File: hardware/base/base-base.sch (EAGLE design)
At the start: 8 parts, among them U1 SD_CARD_SOCKET4UCON, X1 BU-SMA-V

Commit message: BASEHW: Added missing power bits, basically done now
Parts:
- added C1, C4: 22u, SparkFun-Capacitors:CAPPTH
- added C2, C5: 100n, SparkFun-Capacitors:CAPPTH
- added C3, C6: 47u, SparkFun-Capacitors:CAPPTH
- added L1: 2u2, resistor:L-EU0207/7
- added L2: 3u3, resistor:L-EU0207/7
- added R1: 33k2, resistor:R-EU_VMTA55
- added R2, R4: 10k, resistor:R-EU_VMTA55
- added R3: 56k2, resistor:R-EU_VMTA55
- added U$4, U$5: TPS563200, FullyCustom:TPS563200
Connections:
- new net V+: C1.1, C4.1, U$4.EN, U$4.VIN, U$5.VIN
- new net VREG_3_SW: C2.2, L1.1, U$4.SW
- new net VREG_3_VBST: C2.1, U$4.VBST
- new net VREG_3_VFB: R1.1, R2.2, U$4.VFB
- new net VREG_5_SW: C5.2, L2.1, U$5.SW
- new net VREG_5_VBST: C5.1, U$5.VBST
- new net VREG_5_VFB: R3.1, R4.2, U$5.VFB
- net +3V3: now also C3.1, L1.2, R1.2
- net +5V: now also C6.1, L2.2, R3.2
- net GND: now also C1.2, C3.2, C4.2, C6.2, R2.1, R4.1, U$4.GND, U$5.GND
- net GSM_PWR: now also U$1.PD4, U$5.EN
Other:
- note added: "Discovery Board"
- note added: "Subsystems & Power"
- moved on the sheet: Q1, Q2, Q3, U$3, U1, X1

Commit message: BASEHW: Yayy, hardware design done
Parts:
- added C7: 100u, SparkFun-Passives:CAP_POLPTH2
- added DEBUG: (no value), pinhead:PINHD-1X6
- added PWR: (no value), pinhead:PINHD-1X2
- L1, L2: device resistor:L-EU0207/7 -> resistor:L-EU0207/2V
- R1, R2, R3, R4: device resistor:R-EU_VMTA55 -> resistor:R-EU_0204/5
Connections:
- net DEBUG_RX: now also DEBUG.4
- net DEBUG_TX: now also DEBUG.5
- net GND: now also C7.-, DEBUG.1, PWR.2
- net SD_PWR: now also U$1.PB4
- net V+: now also C7.+, PWR.1
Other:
- moved on the sheet: C1, C2, C3, C4, C5, C6, L1, L2, R1, R2, R3, R4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

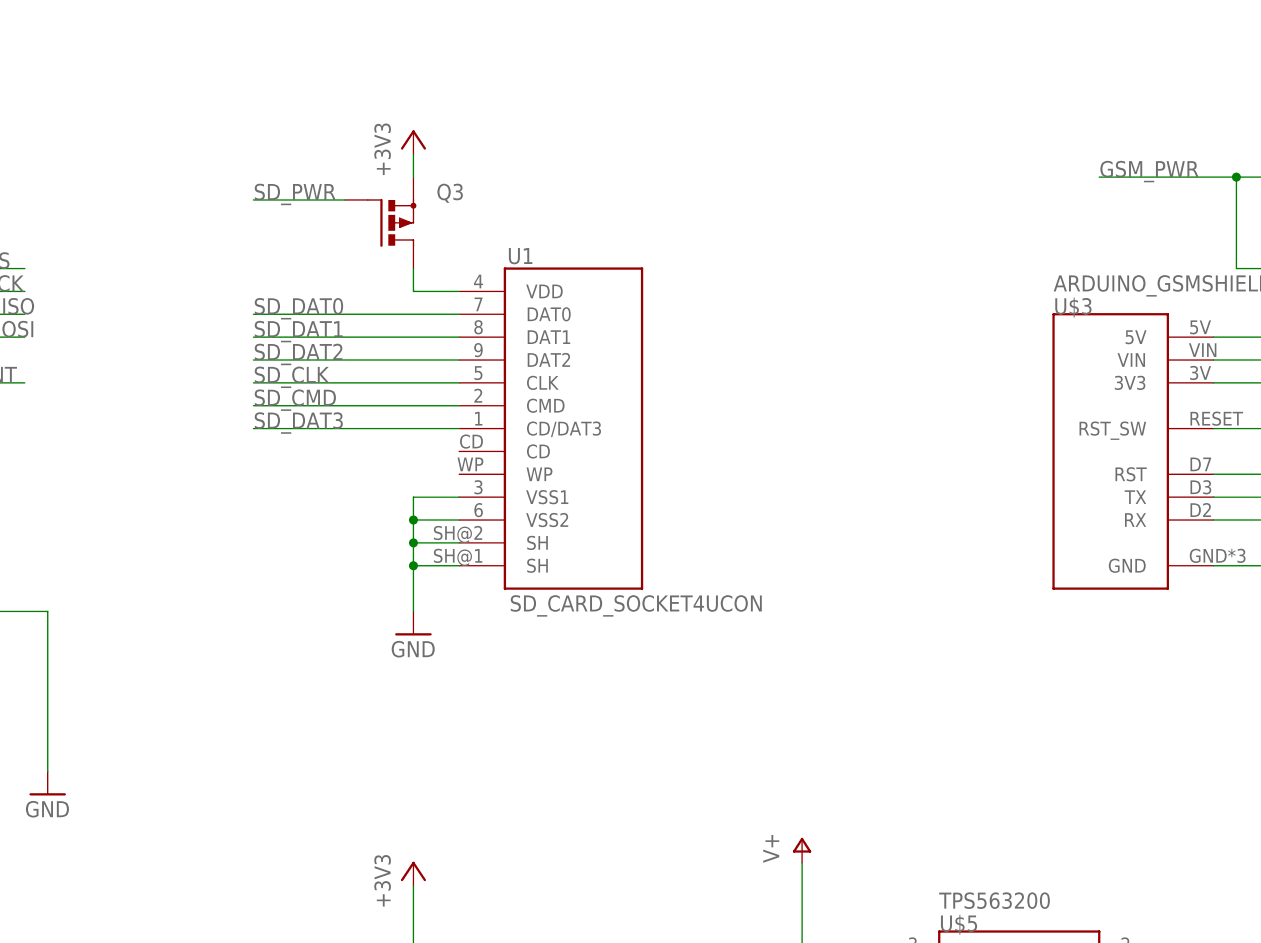
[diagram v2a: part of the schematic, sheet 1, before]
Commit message: BASEHW: Pass for layout bugs, SD pullups
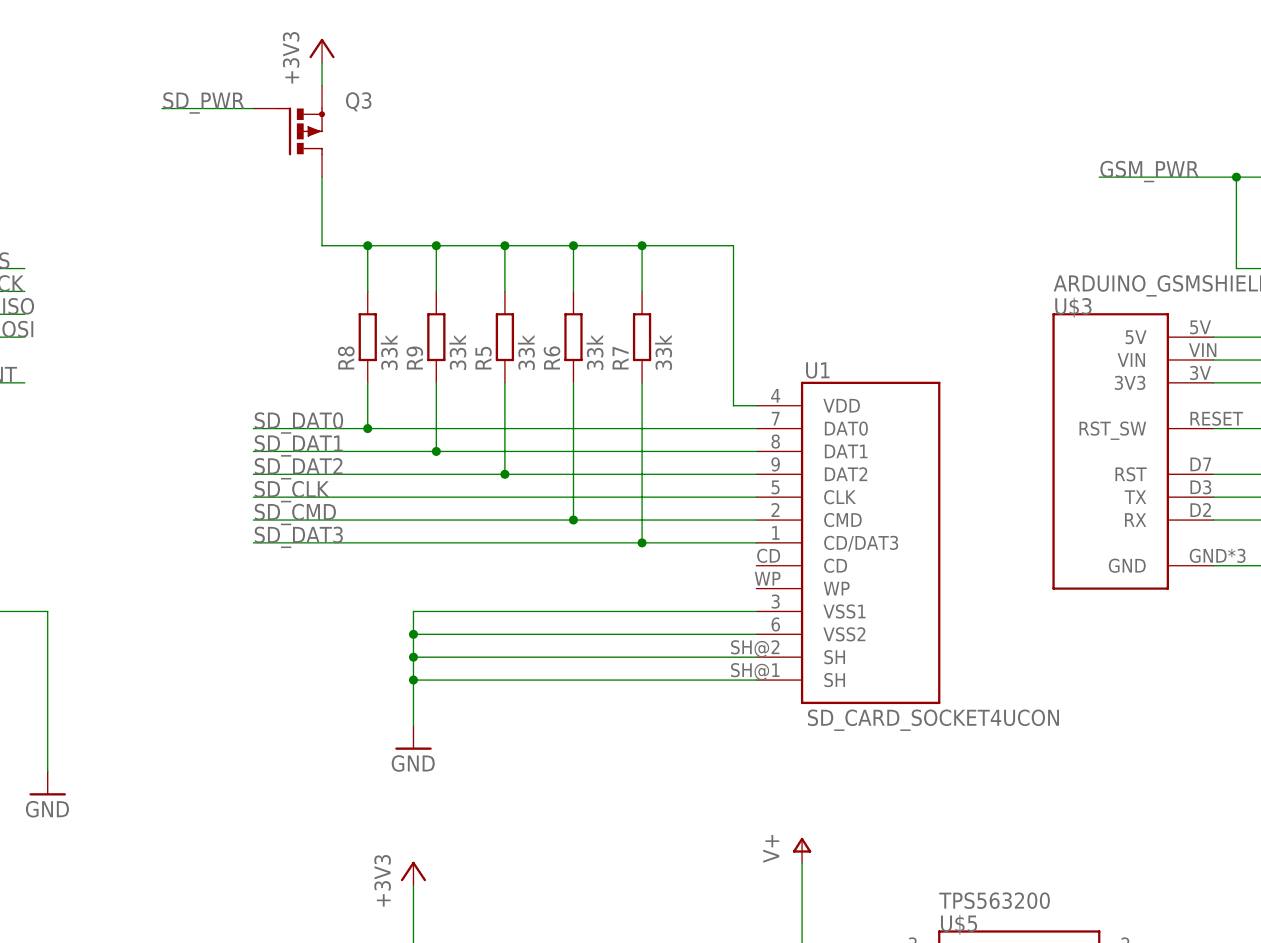
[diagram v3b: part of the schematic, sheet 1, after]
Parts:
- added R5, R6, R7, R8, R9: 33k, resistor:R-EU_0204/5
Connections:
- removed net N$3: Q3.D, U1.VDD
- new net SD_VCC: Q3.D, R5.2, R6.2, R7.2, R8.2, R9.2, U1.VDD
- net SD_CMD: now also R6.1
- net SD_DAT0: now also R8.1
- net SD_DAT1: now also R9.1
- net SD_DAT2: now also R5.1
- net SD_DAT3: now also R7.1
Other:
- moved on the sheet: Q3, U1
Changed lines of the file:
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@@
 <part name="GND10" library="supply1" deviceset="GND" device=""/>
 <part name="C7" library="SparkFun-Passives" deviceset="CAP_POL" device="PTH2" value="100u"/>
+<part name="R5" library="resistor" deviceset="R-EU_" device="0204/5" value="33k"/>
+<part name="R6" library="resistor" deviceset="R-EU_" device="0204/5" value="33k"/>
+<part name="R7" library="resistor" deviceset="R-EU_" device="0204/5" value="33k"/>
+<part name="R8" library="resistor" deviceset="R-EU_" device="0204/5" value="33k"/>
+<part name="R9" library="resistor" deviceset="R-EU_" device="0204/5" value="33k"/>
 </parts>
 <sheets>
@@
 <instance part="GND5" gate="1" x="48.26" y="119.38"/>
 <instance part="X1" gate="G$1" x="15.24" y="142.24"/>
-<instance part="U1" gate="G$1" x="144.78" y="129.54"/>
-<instance part="GND6" gate="1" x="127" y="106.68"/>
-<instance part="+3V6" gate="G$1" x="127" y="162.56"/>
+<instance part="U1" gate="G$1" x="177.8" y="116.84"/>
+<instance part="GND6" gate="1" x="127" y="93.98"/>
+<instance part="+3V6" gate="G$1" x="116.84" y="172.72"/>
 <instance part="U$3" gate="G$1" x="205.74" y="139.7"/>
 <instance part="P+3" gate="1" x="231.14" y="165.1"/>
@@
 <instance part="Q1" gate="G$1" x="228.6" y="154.94"/>
 <instance part="Q2" gate="G$1" x="238.76" y="144.78"/>
-<instance part="Q3" gate="G$1" x="124.46" y="152.4"/>
+<instance part="Q3" gate="G$1" x="114.3" y="162.56"/>
 <instance part="U$4" gate="1" x="58.42" y="68.58"/>
 <instance part="P+4" gate="1" x="48.26" y="81.28"/>
@@
 <instance part="GND10" gate="1" x="86.36" y="88.9"/>
 <instance part="C7" gate="G$1" x="35.56" y="55.88"/>
+<instance part="R5" gate="G$1" x="137.16" y="139.7" rot="R90"/>
+<instance part="R6" gate="G$1" x="144.78" y="139.7" rot="R90"/>
+<instance part="R7" gate="G$1" x="152.4" y="139.7" rot="R90"/>
+<instance part="R8" gate="G$1" x="121.92" y="139.7" rot="R90"/>
+<instance part="R9" gate="G$1" x="129.54" y="139.7" rot="R90"/>
 </instances>
 <busses>
@@
 <pinref part="Q3" gate="G$1" pin="S"/>
 <pinref part="+3V6" gate="G$1" pin="+3V3"/>
-<wire x1="127" y1="157.48" x2="127" y2="160.02" width="0.1524" layer="91"/>
+<wire x1="116.84" y1="167.64" x2="116.84" y2="170.18" width="0.1524" layer="91"/>
 </segment>
 <segment>
@@
 <segment>
 <pinref part="U1" gate="G$1" pin="VSS1"/>
-<wire x1="132.08" y1="121.92" x2="127" y2="121.92" width="0.1524" layer="91"/>
+<wire x1="165.1" y1="109.22" x2="127" y2="109.22" width="0.1524" layer="91"/>
 <pinref part="GND6" gate="1" pin="GND"/>
-<wire x1="127" y1="121.92" x2="127" y2="119.38" width="0.1524" layer="91"/>
+<wire x1="127" y1="109.22" x2="127" y2="106.68" width="0.1524" layer="91"/>
 <pinref part="U1" gate="G$1" pin="VSS2"/>
-<wire x1="127" y1="119.38" x2="127" y2="116.84" width="0.1524" layer="91"/>
-<wire x1="127" y1="116.84" x2="127" y2="114.3" width="0.1524" layer="91"/>
-<wire x1="127" y1="114.3" x2="127" y2="109.22" width="0.1524" layer="91"/>
-<wire x1="132.08" y1="119.38" x2="127" y2="119.38" width="0.1524" layer="91"/>
-<junction x="127" y="119.38"/>
+<wire x1="127" y1="106.68" x2="127" y2="104.14" width="0.1524" layer="91"/>
+<wire x1="127" y1="104.14" x2="127" y2="101.6" width="0.1524" layer="91"/>
+<wire x1="127" y1="101.6" x2="127" y2="96.52" width="0.1524" layer="91"/>
+<wire x1="165.1" y1="106.68" x2="127" y2="106.68" width="0.1524" layer="91"/>
+<junction x="127" y="106.68"/>
 <pinref part="U1" gate="G$1" pin="SH@2"/>
-<wire x1="132.08" y1="116.84" x2="127" y2="116.84" width="0.1524" layer="91"/>
-<junction x="127" y="116.84"/>
+<wire x1="165.1" y1="104.14" x2="127" y2="104.14" width="0.1524" layer="91"/>
+<junction x="127" y="104.14"/>
 <pinref part="U1" gate="G$1" pin="SH@1"/>
-<wire x1="132.08" y1="114.3" x2="127" y2="114.3" width="0.1524" layer="91"/>
-<junction x="127" y="114.3"/>
+<wire x1="165.1" y1="101.6" x2="127" y2="101.6" width="0.1524" layer="91"/>
+<junction x="127" y="101.6"/>
 </segment>
 <segment>
@@
 <segment>
 <pinref part="U1" gate="G$1" pin="DAT0"/>
-<wire x1="132.08" y1="142.24" x2="109.22" y2="142.24" width="0.1524" layer="91"/>
-<label x="109.22" y="142.24" size="1.778" layer="95"/>
+<wire x1="165.1" y1="129.54" x2="121.92" y2="129.54" width="0.1524" layer="91"/>
+<label x="109.22" y="129.54" size="1.778" layer="95"/>
+<pinref part="R8" gate="G$1" pin="1"/>
+<wire x1="121.92" y1="129.54" x2="109.22" y2="129.54" width="0.1524" layer="91"/>
+<wire x1="121.92" y1="134.62" x2="121.92" y2="129.54" width="0.1524" layer="91"/>
+<junction x="121.92" y="129.54"/>
 </segment>
 </net>
@@
 <segment>
 <pinref part="U1" gate="G$1" pin="DAT1"/>
-<wire x1="132.08" y1="139.7" x2="109.22" y2="139.7" width="0.1524" layer="91"/>
-<label x="109.22" y="139.7" size="1.778" layer="95"/>
+<wire x1="165.1" y1="127" x2="129.54" y2="127" width="0.1524" layer="91"/>
+<label x="109.22" y="127" size="1.778" layer="95"/>
+<pinref part="R9" gate="G$1" pin="1"/>
+<wire x1="129.54" y1="127" x2="109.22" y2="127" width="0.1524" layer="91"/>
+<wire x1="129.54" y1="134.62" x2="129.54" y2="127" width="0.1524" layer="91"/>
+<junction x="129.54" y="127"/>
 </segment>
 </net>
@@
 <segment>
 <pinref part="U1" gate="G$1" pin="DAT2"/>
-<wire x1="132.08" y1="137.16" x2="109.22" y2="137.16" width="0.1524" layer="91"/>
-<label x="109.22" y="137.16" size="1.778" layer="95"/>
+<wire x1="165.1" y1="124.46" x2="137.16" y2="124.46" width="0.1524" layer="91"/>
+<label x="109.22" y="124.46" size="1.778" layer="95"/>
+<pinref part="R5" gate="G$1" pin="1"/>
+<wire x1="137.16" y1="124.46" x2="109.22" y2="124.46" width="0.1524" layer="91"/>
+<wire x1="137.16" y1="134.62" x2="137.16" y2="124.46" width="0.1524" layer="91"/>
+<junction x="137.16" y="124.46"/>
 </segment>
 </net>
@@
 <segment>
 <pinref part="U1" gate="G$1" pin="CLK"/>
-<wire x1="132.08" y1="134.62" x2="109.22" y2="134.62" width="0.1524" layer="91"/>
-<label x="109.22" y="134.62" size="1.778" layer="95"/>
+<wire x1="165.1" y1="121.92" x2="109.22" y2="121.92" width="0.1524" layer="91"/>
+<label x="109.22" y="121.92" size="1.778" layer="95"/>
 </segment>
 </net>
@@
 <segment>
 <pinref part="U1" gate="G$1" pin="CMD"/>
-<wire x1="132.08" y1="132.08" x2="109.22" y2="132.08" width="0.1524" layer="91"/>
-<label x="109.22" y="132.08" size="1.778" layer="95"/>
+<wire x1="165.1" y1="119.38" x2="144.78" y2="119.38" width="0.1524" layer="91"/>
+<label x="109.22" y="119.38" size="1.778" layer="95"/>
+<pinref part="R6" gate="G$1" pin="1"/>
+<wire x1="144.78" y1="119.38" x2="109.22" y2="119.38" width="0.1524" layer="91"/>
+<wire x1="144.78" y1="134.62" x2="144.78" y2="119.38" width="0.1524" layer="91"/>
+<junction x="144.78" y="119.38"/>
 </segment>
 </net>
@@
 <segment>
 <pinref part="U1" gate="G$1" pin="CD/DAT3"/>
-<wire x1="132.08" y1="129.54" x2="109.22" y2="129.54" width="0.1524" layer="91"/>
-<label x="109.22" y="129.54" size="1.778" layer="95"/>
+<wire x1="165.1" y1="116.84" x2="152.4" y2="116.84" width="0.1524" layer="91"/>
+<label x="109.22" y="116.84" size="1.778" layer="95"/>
+<pinref part="R7" gate="G$1" pin="1"/>
+<wire x1="152.4" y1="116.84" x2="109.22" y2="116.84" width="0.1524" layer="91"/>
+<wire x1="152.4" y1="134.62" x2="152.4" y2="116.84" width="0.1524" layer="91"/>
+<junction x="152.4" y="116.84"/>
 </segment>
 </net>
@@
 </segment>
 </net>
-<net name="N$3" class="0">
-<segment>
-<pinref part="U1" gate="G$1" pin="VDD"/>
-<wire x1="132.08" y1="144.78" x2="127" y2="144.78" width="0.1524" layer="91"/>
-<pinref part="Q3" gate="G$1" pin="D"/>
-<wire x1="127" y1="147.32" x2="127" y2="144.78" width="0.1524" layer="91"/>
-</segment>
-</net>
 <net name="SD_PWR" class="0">
 <segment>
 <pinref part="Q3" gate="G$1" pin="G"/>
-<wire x1="119.38" y1="154.94" x2="109.22" y2="154.94" width="0.1524" layer="91"/>
-<label x="109.22" y="154.94" size="1.778" layer="95"/>
+<wire x1="109.22" y1="165.1" x2="99.06" y2="165.1" width="0.1524" layer="91"/>
+<label x="99.06" y="165.1" size="1.778" layer="95"/>
 </segment>
 </net>
@@
 </segment>
 </net>
+<net name="SD_VCC" class="0">
+<segment>
+<pinref part="R8" gate="G$1" pin="2"/>
+<pinref part="Q3" gate="G$1" pin="D"/>
+<wire x1="116.84" y1="157.48" x2="116.84" y2="149.86" width="0.1524" layer="91"/>
+<wire x1="116.84" y1="149.86" x2="121.92" y2="149.86" width="0.1524" layer="91"/>
+<wire x1="121.92" y1="149.86" x2="129.54" y2="149.86" width="0.1524" layer="91"/>
+<wire x1="129.54" y1="149.86" x2="137.16" y2="149.86" width="0.1524" layer="91"/>
+<wire x1="137.16" y1="149.86" x2="144.78" y2="149.86" width="0.1524" layer="91"/>
+<wire x1="144.78" y1="149.86" x2="152.4" y2="149.86" width="0.1524" layer="91"/>
+<wire x1="152.4" y1="149.86" x2="162.56" y2="149.86" width="0.1524" layer="91"/>
+<wire x1="162.56" y1="149.86" x2="162.56" y2="132.08" width="0.1524" layer="91"/>
+<pinref part="U1" gate="G$1" pin="VDD"/>
+<wire x1="162.56" y1="132.08" x2="165.1" y2="132.08" width="0.1524" layer="91"/>
+<pinref part="R7" gate="G$1" pin="2"/>
+<wire x1="152.4" y1="144.78" x2="152.4" y2="149.86" width="0.1524" layer="91"/>
+<junction x="152.4" y="149.86"/>
+<pinref part="R6" gate="G$1" pin="2"/>
+<wire x1="144.78" y1="144.78" x2="144.78" y2="149.86" width="0.1524" layer="91"/>
+<junction x="144.78" y="149.86"/>
+<pinref part="R5" gate="G$1" pin="2"/>
+<wire x1="137.16" y1="144.78" x2="137.16" y2="149.86" width="0.1524" layer="91"/>
+<junction x="137.16" y="149.86"/>
+<pinref part="R9" gate="G$1" pin="2"/>
+<wire x1="129.54" y1="144.78" x2="129.54" y2="149.86" width="0.1524" layer="91"/>
+<junction x="129.54" y="149.86"/>
+<wire x1="121.92" y1="144.78" x2="121.92" y2="149.86" width="0.1524" layer="91"/>
+<junction x="121.92" y="149.86"/>
+</segment>
+</net>
